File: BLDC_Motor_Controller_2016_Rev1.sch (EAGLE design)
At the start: 98 parts, among them Q1 MOSFET-NCHANNELFQP30N06L, Q2 MOSFET-NCHANNELFQP30N06L, Q3 MOSFET-NCHANNELFQP30N06L, Q4 MOSFET-NCHANNELFQP30N06L, Q5 MOSFET-NCHANNELFQP30N06L, Q6 MOSFET-NCHANNELFQP30N06L, Q7 MOSFET-PCHANNEL, Q8 MOSFET-PCHANNEL

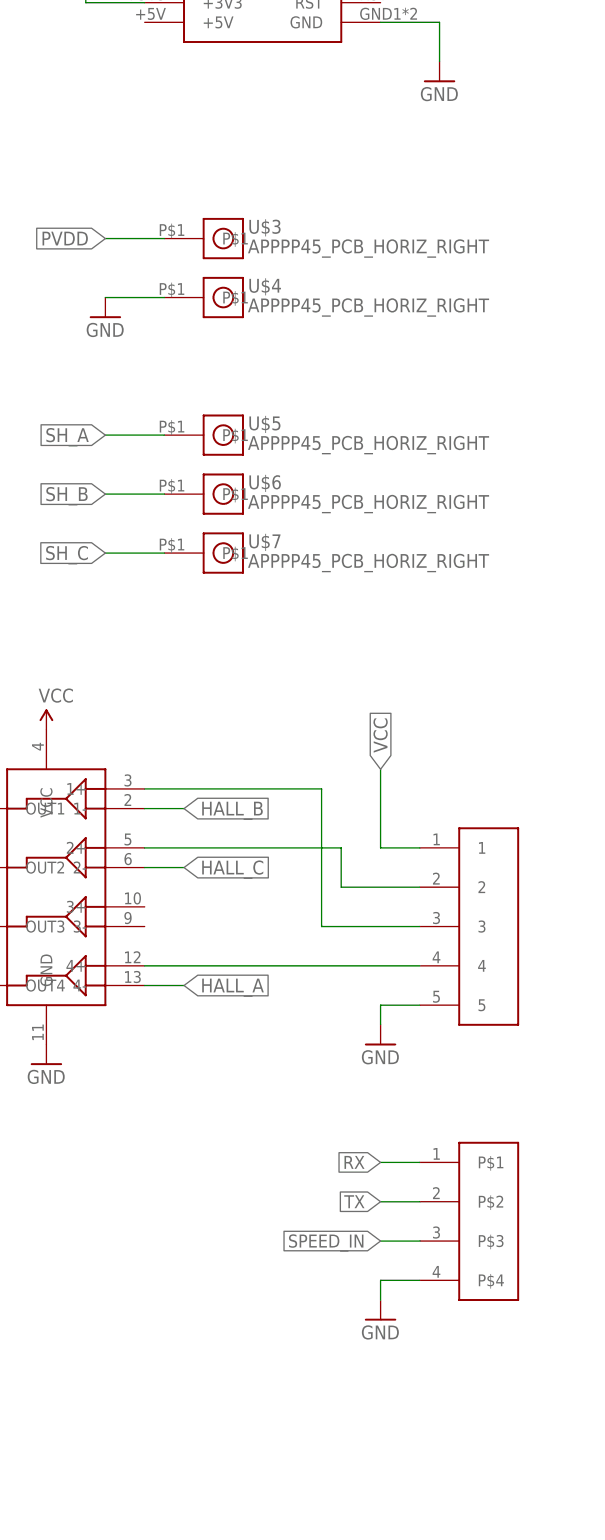
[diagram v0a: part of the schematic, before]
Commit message: Swapped SL connectors, added APP spacer
Swapped 4-pin Molex SL for two 3-pin SL connectors, added mounting wing
between power inputs, added board description and MRDT logo, moved big
caps around
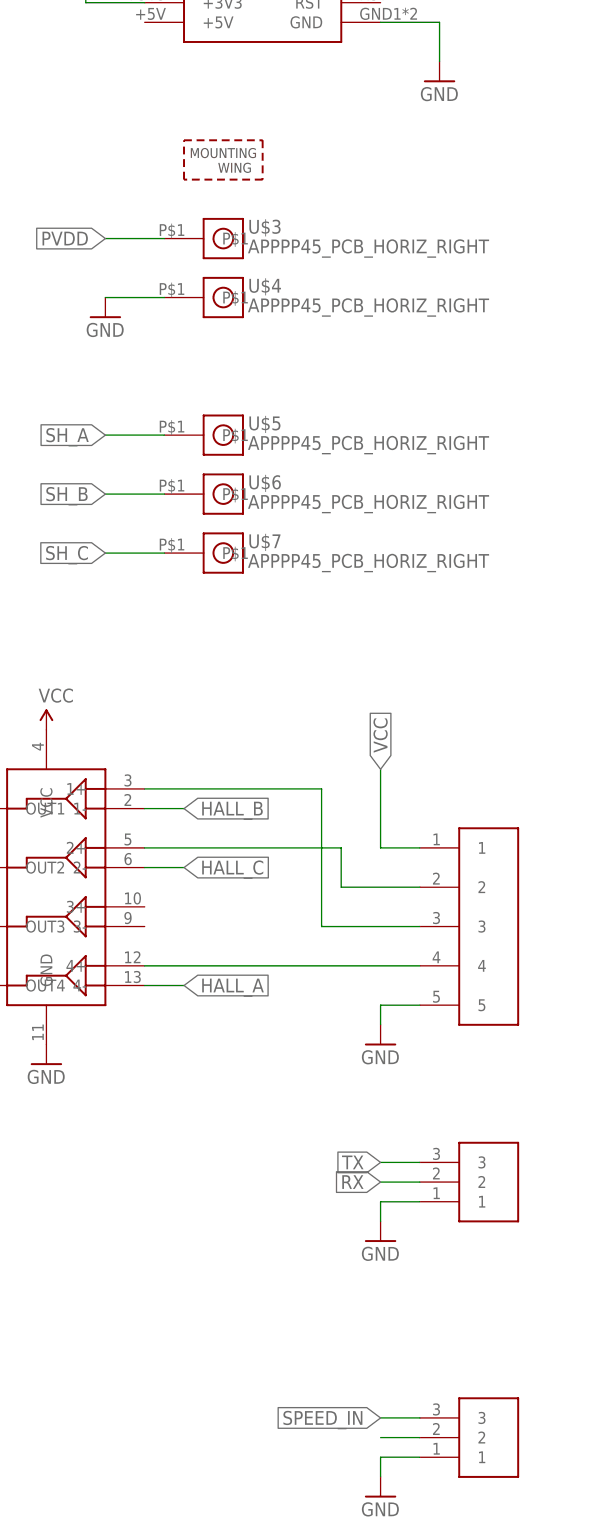
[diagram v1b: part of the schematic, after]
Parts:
- removed U$9: 4PIN, Molex-SL:4PIN
- added J1, J2: SL03THROUGH_HOLE, MRDT-Connectors:SL03THROUGH_HOLE
- added U$10: APP_MOUTING_WINGHORIZ, MRDT-Connectors:APP_MOUTING_WINGHORIZ
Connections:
- new net N$36: J1.2
- net GND: now also J1.1, J2.1; no longer U$9.P$4
- net RX: now also J2.2; no longer U$9.P$1
- net SPEED_IN: now also J1.3; no longer U$9.P$3
- net TX: now also J2.3; no longer U$9.P$2
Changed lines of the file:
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@@
 <?xml version="1.0" encoding="utf-8"?>
 <!DOCTYPE eagle SYSTEM "eagle.dtd">
-<eagle version="7.4.0">
+<eagle version="7.3.0">
 <drawing>
 <settings>
@@
 <layer number="128" name="_bValues" color="7" fill="1" visible="yes" active="yes"/>
 <layer number="129" name="Mask" color="7" fill="1" visible="yes" active="yes"/>
+<layer number="130" name="130bmp" color="7" fill="1" visible="yes" active="yes"/>
 <layer number="131" name="tAdjust" color="7" fill="1" visible="yes" active="yes"/>
 <layer number="132" name="bAdjust" color="7" fill="1" visible="yes" active="yes"/>
@@
 <layer number="143" name="PMD" color="7" fill="1" visible="no" active="yes"/>
 <layer number="144" name="Drill_legend" color="7" fill="1" visible="yes" active="yes"/>
+<layer number="145" name="DrillLegend_01-16" color="7" fill="1" visible="yes" active="yes"/>
 <layer number="150" name="Notes" color="7" fill="1" visible="yes" active="yes"/>
 <layer number="151" name="HeatSink" color="7" fill="1" visible="yes" active="yes"/>
@@
 <part name="GND33" library="SparkFun-Aesthetics" deviceset="GND" device=""/>
 <part name="U$14" library="Inductor_DR74" deviceset="INDUCTOR_DR74" device="" value="33u"/>
-<part name="GND34" library="SparkFun-Aesthetics" deviceset="GND" device=""/>
 <part name="U$8" library="Molex-SL" deviceset="5PIN" device=""/>
-<part name="U$9" library="Molex-SL" deviceset="4PIN" device=""/>
 <part name="R13" library="SparkFun-Passives" deviceset="RESISTOR" device="1206" value=".001"/>
 <part name="R18" library="SparkFun-Passives" deviceset="RESISTOR" device="1206" value=".001"/>
 <part name="C34" library="SparkFun-Passives" deviceset="CAP_POL" device="PTH4" value="220u"/>
 <part name="C35" library="SparkFun-Passives" deviceset="CAP_POL" device="PTH4" value="220u"/>
+<part name="U$10" library="MRDT-Connectors" deviceset="APP_MOUTING_WING" device="HORIZ"/>
+<part name="J1" library="MRDT-Connectors" deviceset="SL03" device="THROUGH_HOLE"/>
+<part name="GND35" library="SparkFun-Aesthetics" deviceset="GND" device=""/>
+<part name="J2" library="MRDT-Connectors" deviceset="SL03" device="THROUGH_HOLE"/>
+<part name="GND34" library="SparkFun-Aesthetics" deviceset="GND" device=""/>
 </parts>
 <sheets>
@@
 <instance part="GND33" gate="1" x="233.68" y="-152.4"/>
 <instance part="U$14" gate="G$1" x="48.26" y="50.8"/>
-<instance part="GND34" gate="1" x="276.86" y="-185.42"/>
 <instance part="U$8" gate="G$1" x="289.56" y="-137.16"/>
-<instance part="U$9" gate="G$1" x="289.56" y="-172.72"/>
 <instance part="R13" gate="G$1" x="142.24" y="12.7" rot="R90"/>
 <instance part="R18" gate="G$1" x="142.24" y="-68.58" rot="R90"/>
 <instance part="C34" gate="G$1" x="-53.34" y="-121.92"/>
 <instance part="C35" gate="G$1" x="-63.5" y="-121.92"/>
+<instance part="U$10" gate="G$1" x="251.46" y="-38.1"/>
+<instance part="J1" gate="G$1" x="289.56" y="-200.66"/>
+<instance part="GND35" gate="1" x="276.86" y="-208.28"/>
+<instance part="J2" gate="G$1" x="289.56" y="-167.64"/>
+<instance part="GND34" gate="1" x="276.86" y="-175.26"/>
 </instances>
 <busses>
@@
 </segment>
 <segment>
-<wire x1="281.94" y1="-180.34" x2="276.86" y2="-180.34" width="0.1524" layer="91"/>
-<wire x1="276.86" y1="-180.34" x2="276.86" y2="-182.88" width="0.1524" layer="91"/>
-<pinref part="GND34" gate="1" pin="GND"/>
-<pinref part="U$9" gate="G$1" pin="P$4"/>
-</segment>
-<segment>
 <wire x1="142.24" y1="-73.66" x2="142.24" y2="-78.74" width="0.1524" layer="91"/>
 <wire x1="142.24" y1="-73.66" x2="129.54" y2="-73.66" width="0.1524" layer="91"/>
@@
 <pinref part="Q6" gate="G$1" pin="S"/>
 <wire x1="142.24" y1="-144.78" x2="142.24" y2="-134.62" width="0.1524" layer="91"/>
+</segment>
+<segment>
+<pinref part="J1" gate="G$1" pin="1"/>
+<wire x1="281.94" y1="-203.2" x2="276.86" y2="-203.2" width="0.1524" layer="91"/>
+<pinref part="GND35" gate="1" pin="GND"/>
+<wire x1="276.86" y1="-203.2" x2="276.86" y2="-205.74" width="0.1524" layer="91"/>
+</segment>
+<segment>
+<pinref part="J2" gate="G$1" pin="1"/>
+<wire x1="281.94" y1="-170.18" x2="276.86" y2="-170.18" width="0.1524" layer="91"/>
+<wire x1="276.86" y1="-170.18" x2="276.86" y2="-172.72" width="0.1524" layer="91"/>
+<pinref part="GND34" gate="1" pin="GND"/>
 </segment>
 </net>
@@
 <net name="TX" class="0">
 <segment>
-<wire x1="281.94" y1="-170.18" x2="276.86" y2="-170.18" width="0.1524" layer="91"/>
-<label x="276.86" y="-170.18" size="1.6764" layer="95" rot="R180" xref="yes"/>
-<pinref part="U$9" gate="G$1" pin="P$2"/>
-</segment>
-<segment>
 <pinref part="U$2" gate="G$1" pin="PB1"/>
 <wire x1="276.86" y1="38.1" x2="284.48" y2="38.1" width="0.1524" layer="91"/>
 <label x="284.48" y="38.1" size="1.6764" layer="95" xref="yes"/>
 </segment>
+<segment>
+<pinref part="J2" gate="G$1" pin="3"/>
+<wire x1="281.94" y1="-165.1" x2="276.86" y2="-165.1" width="0.1524" layer="91"/>
+<label x="276.86" y="-165.1" size="1.778" layer="95" rot="R180" xref="yes"/>
+</segment>
 </net>
 <net name="RX" class="0">
-<segment>
-<wire x1="281.94" y1="-165.1" x2="276.86" y2="-165.1" width="0.1524" layer="91"/>
-<label x="276.86" y="-165.1" size="1.6764" layer="95" rot="R180" xref="yes"/>
-<pinref part="U$9" gate="G$1" pin="P$1"/>
-</segment>
 <segment>
 <pinref part="U$2" gate="G$1" pin="PB0"/>
@@
 <label x="284.48" y="40.64" size="1.6764" layer="95" xref="yes"/>
 </segment>
+<segment>
+<pinref part="J2" gate="G$1" pin="2"/>
+<wire x1="281.94" y1="-167.64" x2="276.86" y2="-167.64" width="0.1524" layer="91"/>
+<label x="276.86" y="-167.64" size="1.778" layer="95" rot="R180" xref="yes"/>
+</segment>
 </net>
 <net name="SPEED_IN" class="0">
@@
 </segment>
 <segment>
-<wire x1="281.94" y1="-175.26" x2="276.86" y2="-175.26" width="0.1524" layer="91"/>
-<label x="276.86" y="-175.26" size="1.6764" layer="95" rot="R180" xref="yes"/>
-<pinref part="U$9" gate="G$1" pin="P$3"/>
-</segment>
-</net>
+<pinref part="J1" gate="G$1" pin="3"/>
+<wire x1="281.94" y1="-198.12" x2="276.86" y2="-198.12" width="0.1524" layer="91"/>
+<label x="276.86" y="-198.12" size="1.778" layer="95" rot="R180" xref="yes"/>
+</segment>
+</net>
+<net name="N$36" class="0">
+<segment>
+<pinref part="J1" gate="G$1" pin="2"/>
+<wire x1="281.94" y1="-200.66" x2="276.86" y2="-200.66" width="0.1524" layer="91"/>
+</segment>
+</net>

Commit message: Swapped side-by-side anderson input with stacked orientation
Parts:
- removed U$10: APP_MOUTING_WINGHORIZ, MRDT-Connectors:APP_MOUTING_WINGHORIZ
- removed U$3, U$4: APPPP45_PCB_HORIZ_RIGHT, MRDT-Connectors:APPPP45_PCB_HORIZ_RIGHT
- added C38: 220u, SparkFun-Passives:CAP_POLPTH4
- added J3: APP_2POS_CONFIG5V_HORIZ, MRDT-Connectors:APP_2POS_CONFIG5V_HORIZ
- J1: value SL03THROUGH_HOLE -> SERVOMOLEX_SL_THRU_HOLE; device MRDT-Connectors:SL03THROUGH_HOLE -> MRDT-Connectors:SERVOMOLEX_SL_THRU_HOLE
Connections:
- removed net N$36: J1.2
- net GND: now also C38.-, J1.GND, J3GND.P$1; no longer J1.1, U$4.P$1
- net PVDD: now also C38.+, J3VCC.P$1; no longer U$3.P$1
- net SPEED_IN: now also J1.SIG; no longer J1.3
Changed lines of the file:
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@@
 <part name="GND31" library="SparkFun-Aesthetics" deviceset="GND" device=""/>
 <part name="GND32" library="SparkFun-Aesthetics" deviceset="GND" device=""/>
-<part name="U$3" library="MRDT-Connectors" deviceset="APP" device="PP45_PCB_HORIZ_RIGHT"/>
-<part name="U$4" library="MRDT-Connectors" deviceset="APP" device="PP45_PCB_HORIZ_RIGHT"/>
 <part name="U$5" library="MRDT-Connectors" deviceset="APP" device="PP45_PCB_HORIZ_RIGHT"/>
 <part name="U$6" library="MRDT-Connectors" deviceset="APP" device="PP45_PCB_HORIZ_RIGHT"/>
@@
 <part name="C34" library="SparkFun-Passives" deviceset="CAP_POL" device="PTH4" value="220u"/>
 <part name="C35" library="SparkFun-Passives" deviceset="CAP_POL" device="PTH4" value="220u"/>
-<part name="U$10" library="MRDT-Connectors" deviceset="APP_MOUTING_WING" device="HORIZ"/>
-<part name="J1" library="MRDT-Connectors" deviceset="SL03" device="THROUGH_HOLE"/>
 <part name="GND35" library="SparkFun-Aesthetics" deviceset="GND" device=""/>
 <part name="J2" library="MRDT-Connectors" deviceset="SL03" device="THROUGH_HOLE"/>
 <part name="GND34" library="SparkFun-Aesthetics" deviceset="GND" device=""/>
+<part name="J1" library="MRDT-Connectors" deviceset="SERVO" device="MOLEX_SL_THRU_HOLE"/>
+<part name="J3" library="MRDT-Connectors" deviceset="APP_2POS_CONFIG" device="5V_HORIZ"/>
+<part name="C38" library="SparkFun-Passives" deviceset="CAP_POL" device="PTH4" value="220u"/>
 </parts>
 <sheets>
@@
 <instance part="GND31" gate="1" x="-134.62" y="-43.18"/>
 <instance part="GND32" gate="1" x="-106.68" y="-43.18"/>
-<instance part="U$3" gate="G$1" x="256.54" y="-45.72"/>
-<instance part="U$4" gate="G$1" x="256.54" y="-53.34"/>
 <instance part="U$5" gate="G$1" x="256.54" y="-71.12"/>
 <instance part="U$6" gate="G$1" x="256.54" y="-78.74"/>
@@
 <instance part="C34" gate="G$1" x="-53.34" y="-121.92"/>
 <instance part="C35" gate="G$1" x="-63.5" y="-121.92"/>
-<instance part="U$10" gate="G$1" x="251.46" y="-38.1"/>
-<instance part="J1" gate="G$1" x="289.56" y="-200.66"/>
-<instance part="GND35" gate="1" x="276.86" y="-208.28"/>
+<instance part="GND35" gate="1" x="274.32" y="-195.58"/>
 <instance part="J2" gate="G$1" x="289.56" y="-167.64"/>
 <instance part="GND34" gate="1" x="276.86" y="-175.26"/>
+<instance part="J1" gate="G$1" x="284.48" y="-193.04"/>
+<instance part="J3" gate="GND" x="256.54" y="-53.34"/>
+<instance part="J3" gate="VCC" x="256.54" y="-45.72"/>
+<instance part="C38" gate="G$1" x="-73.66" y="-121.92"/>
 </instances>
 <busses>
@@
 <wire x1="-53.34" y1="-127" x2="-53.34" y2="-137.16" width="0.1524" layer="91"/>
 <junction x="-53.34" y="-137.16"/>
+<pinref part="C38" gate="G$1" pin="-"/>
+<wire x1="-73.66" y1="-127" x2="-73.66" y2="-137.16" width="0.1524" layer="91"/>
+<wire x1="-73.66" y1="-137.16" x2="-63.5" y2="-137.16" width="0.1524" layer="91"/>
+<junction x="-63.5" y="-137.16"/>
 </segment>
 <segment>
@@
 </segment>
 <segment>
-<pinref part="U$4" gate="G$1" pin="P$1"/>
 <wire x1="248.92" y1="-53.34" x2="241.3" y2="-53.34" width="0.1524" layer="91"/>
 <pinref part="GND27" gate="1" pin="GND"/>
+<pinref part="J3" gate="GND" pin="P$1"/>
 </segment>
 <segment>
@@
 </segment>
 <segment>
-<pinref part="J1" gate="G$1" pin="1"/>
-<wire x1="281.94" y1="-203.2" x2="276.86" y2="-203.2" width="0.1524" layer="91"/>
+<wire x1="279.4" y1="-190.5" x2="274.32" y2="-190.5" width="0.1524" layer="91"/>
 <pinref part="GND35" gate="1" pin="GND"/>
-<wire x1="276.86" y1="-203.2" x2="276.86" y2="-205.74" width="0.1524" layer="91"/>
+<wire x1="274.32" y1="-190.5" x2="274.32" y2="-193.04" width="0.1524" layer="91"/>
+<pinref part="J1" gate="G$1" pin="GND"/>
 </segment>
 <segment>
@@
 <wire x1="-53.34" y1="-119.38" x2="-53.34" y2="-114.3" width="0.1524" layer="91"/>
 <junction x="-53.34" y="-114.3"/>
+<pinref part="C38" gate="G$1" pin="+"/>
+<wire x1="-63.5" y1="-114.3" x2="-73.66" y2="-114.3" width="0.1524" layer="91"/>
+<wire x1="-73.66" y1="-114.3" x2="-73.66" y2="-119.38" width="0.1524" layer="91"/>
+<junction x="-63.5" y="-114.3"/>
 </segment>
 <segment>
@@
 </segment>
 <segment>
-<pinref part="U$3" gate="G$1" pin="P$1"/>
 <wire x1="248.92" y1="-45.72" x2="241.3" y2="-45.72" width="0.1524" layer="91"/>
 <label x="241.3" y="-45.72" size="1.778" layer="95" rot="R180" xref="yes"/>
+<pinref part="J3" gate="VCC" pin="P$1"/>
 </segment>
 </net>
@@
 </segment>
 <segment>
-<pinref part="J1" gate="G$1" pin="3"/>
-<wire x1="281.94" y1="-198.12" x2="276.86" y2="-198.12" width="0.1524" layer="91"/>
-<label x="276.86" y="-198.12" size="1.778" layer="95" rot="R180" xref="yes"/>
-</segment>
-</net>
-<net name="N$36" class="0">
-<segment>
-<pinref part="J1" gate="G$1" pin="2"/>
-<wire x1="281.94" y1="-200.66" x2="276.86" y2="-200.66" width="0.1524" layer="91"/>
-</segment>
-</net>
+<wire x1="279.4" y1="-187.96" x2="274.32" y2="-187.96" width="0.1524" layer="91"/>
+<label x="274.32" y="-187.96" size="1.778" layer="95" rot="R180" xref="yes"/>
+<pinref part="J1" gate="G$1" pin="SIG"/>
+</segment>
+</net>
